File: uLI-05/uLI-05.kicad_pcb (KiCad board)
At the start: 2 copper layers, 58 x 39.5 mm, 51 parts, among them J1 STL1550, J2 USB_B, J3 RJ25, J4 RJ25, J5 PROG, Q1 IRF7306, U1 LM78M05_TO252, U2 PC817, U3 PC817, U4 PIC18F14K50-EP, U5 ADM2483xRW, U6 USBLC6-2SC6, Y1 12MHz

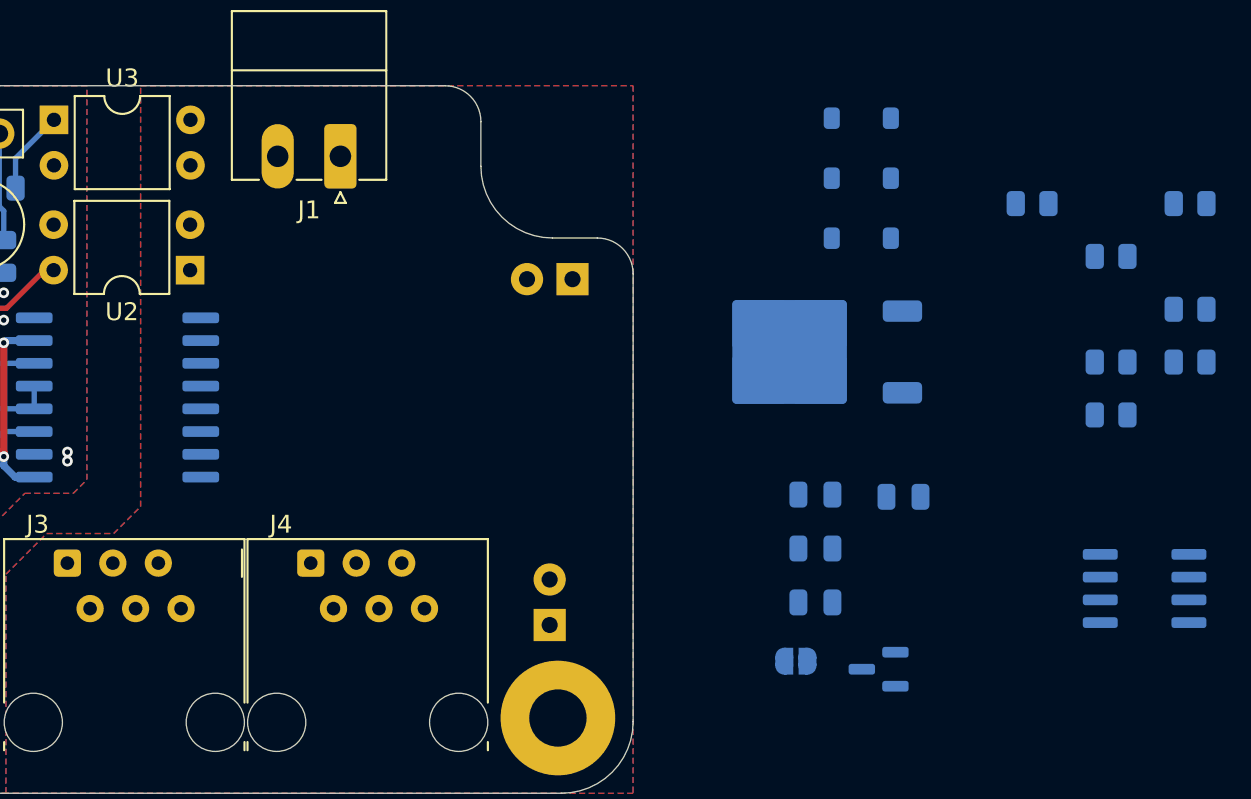
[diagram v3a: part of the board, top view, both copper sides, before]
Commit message: pcb: wire XpressNET part.
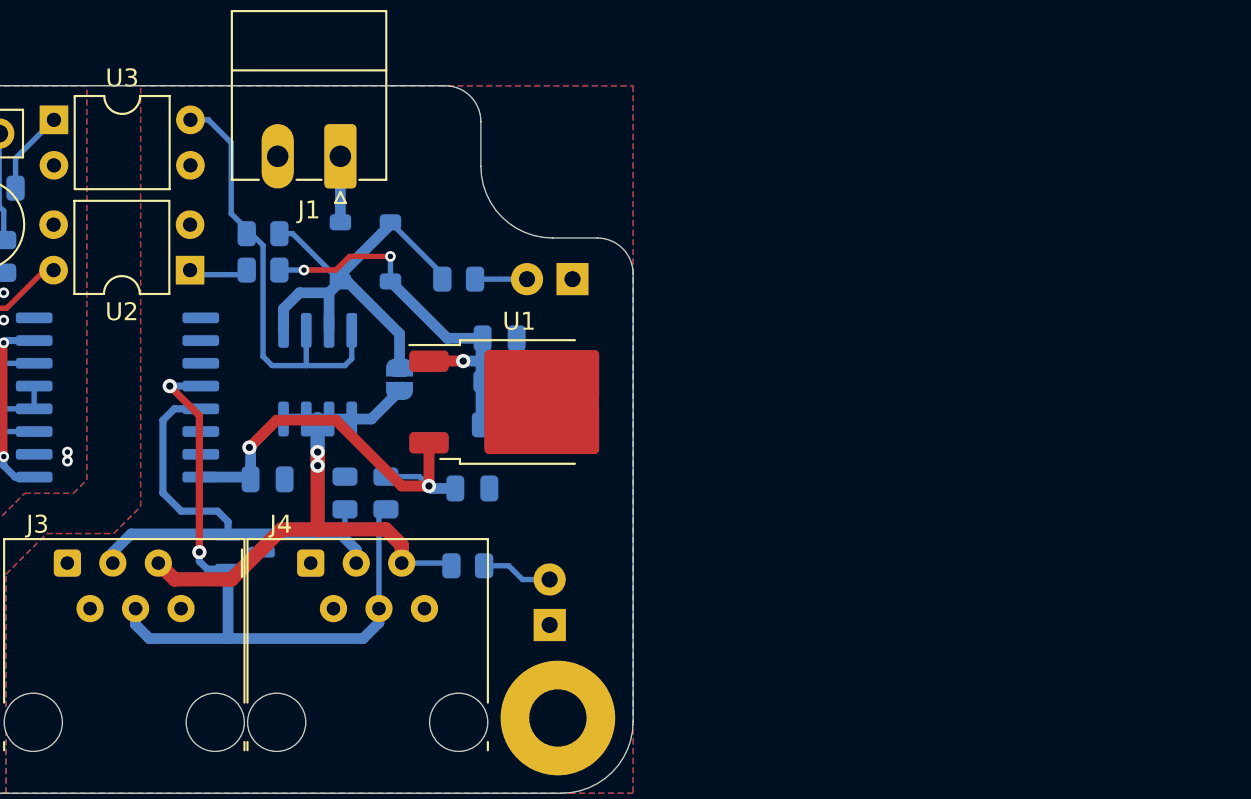
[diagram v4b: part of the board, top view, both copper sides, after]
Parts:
- U1: moved to F.Cu
- moved R1 51.9 mm to (163.7, 92.7), turned to 0 degrees
- moved R10 47.9 mm to (163.7, 90.7)
- moved R4 47.7 mm to (168.3, 105.2), turned to 90 degrees
- moved Q1 47.7 mm to (166.8, 98.6), turned to -90 degrees
- moved R3 46.1 mm to (170.6, 105.2), turned to -90 degrees
- moved R11 36.9 mm to (175.1, 109.2), turned to 0 degrees
- moved R8 36.4 mm to (174.6, 93.2), turned to 0 degrees
- moved D7 36.0 mm to (162.7, 108.5), turned to 0 degrees
- moved C6 35.5 mm to (164.0, 104.4), turned to 0 degrees
- moved R13 32.3 mm to (176.8, 101.4), turned to 0 degrees
- moved D2 29.4 mm to (168.0, 91.7), turned to 90 degrees
- moved D1 27.3 mm to (170.8, 91.7), turned to 90 degrees
- moved JP1 27.2 mm to (171.3, 98.8), turned to 90 degrees
- moved D3 21.1 mm to (177.6, 99.0), turned to 0 degrees
- moved C7 19.7 mm to (176.9, 96.5), turned to 0 degrees
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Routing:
- net /A: track 0.00 -> 39.6 mm, vias 0 -> 2
- net /12VXN: track 0.00 -> 33.4 mm, vias 0 -> 2
- net /B: track 0.00 -> 28.7 mm
- net +12VA: track 0.00 -> 26.9 mm
- net /POWERA: track 0.00 -> 24.4 mm
- net +5VA: track 0.00 -> 23.4 mm, vias 0 -> 2
- net Net-(D1-K): track 0.00 -> 22.1 mm, vias 0 -> 3
- net Net-(D3-A): track 0.00 -> 4.37 mm
- net Net-(D5-A): track 0.00 -> 3.98 mm
- net Net-(D2-A): track 0.00 -> 3.68 mm
- net Net-(R1-Pad1): track 0.00 -> 3.26 mm
- net Net-(D4-A): track 0.00 -> 2.90 mm
